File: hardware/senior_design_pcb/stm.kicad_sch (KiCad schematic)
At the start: 53 parts, among them J1 SBH11-PBPC-D05-ST-BK, J10 1x03 Socket, J2 USB_C_Receptacle_USB2.0_16P, J3 1x03 Socket, J4 Conn_01x03_Socket, J5 1x03 Socket, J6 Screw_Terminal_01x06, J7 Screw_Terminal_01x06, J8 Conn_02x08_Odd_Even, J9 Conn_01x03_Socket, SW1 SW_Push, SW2 SW_Push, U1 FT232RL, U2 STM32F091RCTx, U3 LD1117S33TR_SOT223, X1 32.768kHz(12.5pF), X2 8MHz(20pF)

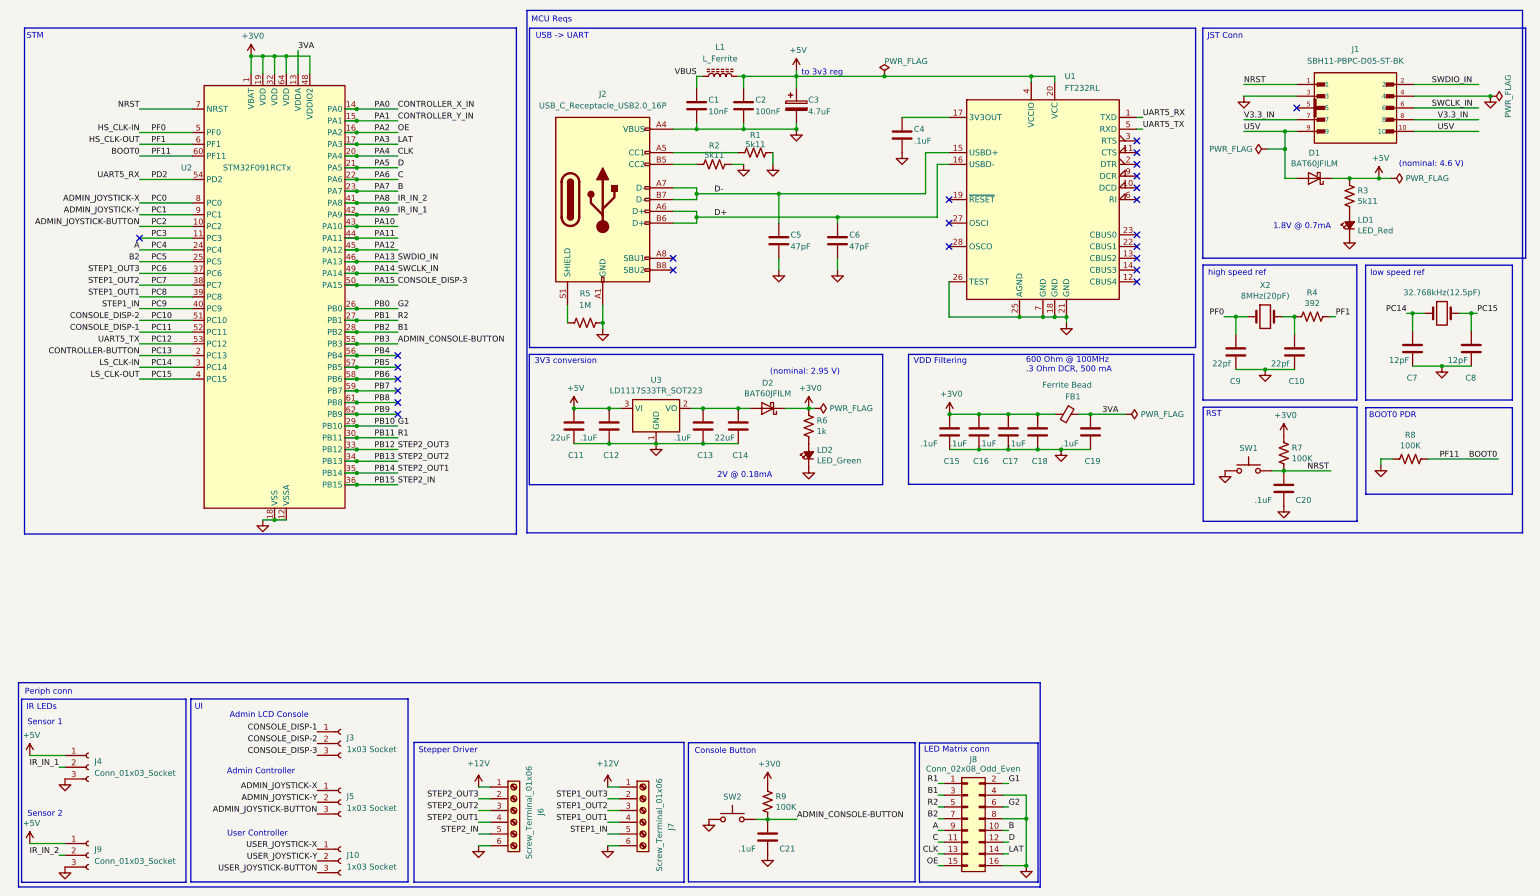
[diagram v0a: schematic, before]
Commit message: vdd caps edited
apparently 362 gaslight us and they dont have the ones we need so i added more :(
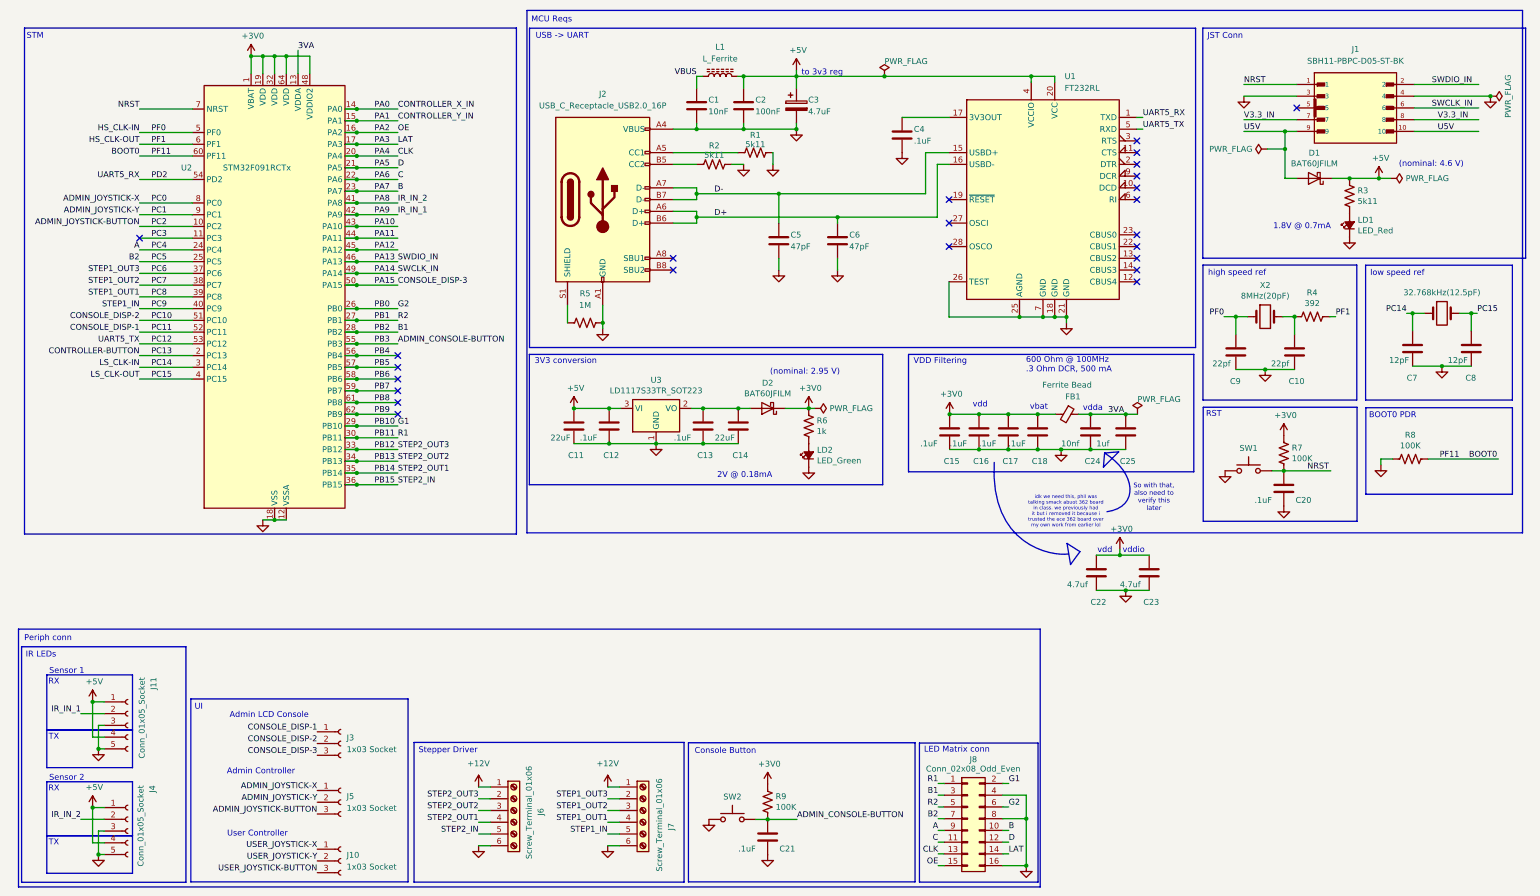
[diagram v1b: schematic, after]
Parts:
- removed C19: .1uF, Capacitor_SMD:C_0805_2012Metric_Pad1.15x1.40mm_HandSolder, symbol Device:C
- removed J4, J9: Conn_01x03_Socket, symbol Connector:Conn_01x03_Socket
- added C22, C23: 4.7uf, Capacitor_SMD:C_0805_2012Metric_Pad1.15x1.40mm_HandSolder, symbol Device:C
- added C24: 10nf, Capacitor_SMD:C_0805_2012Metric_Pad1.15x1.40mm_HandSolder, symbol Device:C
- added C25: 1uf, Capacitor_SMD:C_0805_2012Metric_Pad1.15x1.40mm_HandSolder, symbol Device:C
- added J11, J4: Conn_01x05_Socket, symbol Connector:Conn_01x05_Socket
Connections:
- net +3V0: now also C22.1, C23.1
- net +5V: now also J11.1 (Pin_1), J11.4 (Pin_4), J4.1 (Pin_1), J4.4 (Pin_4)
- net 3VA: now also C24.1, C25.1
- net GND: now also C22.2, C23.2, C24.2, C25.2, J11.3 (Pin_3), J11.5 (Pin_5), J4.3 (Pin_3), J4.5 (Pin_5)
- net IR_IN_1: now also J11.2 (Pin_2)
- net IR_IN_2: now also J4.2 (Pin_2)
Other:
- note added: "RX"
- note added: "So with that, also need to verify this later"
- note added: "TX"
- note added: "idk we need this, phil was talking smack abuot 362 board in class. we previously had it but i removed it because i trusted the ece 362 board over my own work from earlier lol"
- note added: "vbat"
- note added: "vdd"
- note added: "vdd vddio"
- note added: "vdda"

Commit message: fixed connectors
apparently things need power so I added pins for that
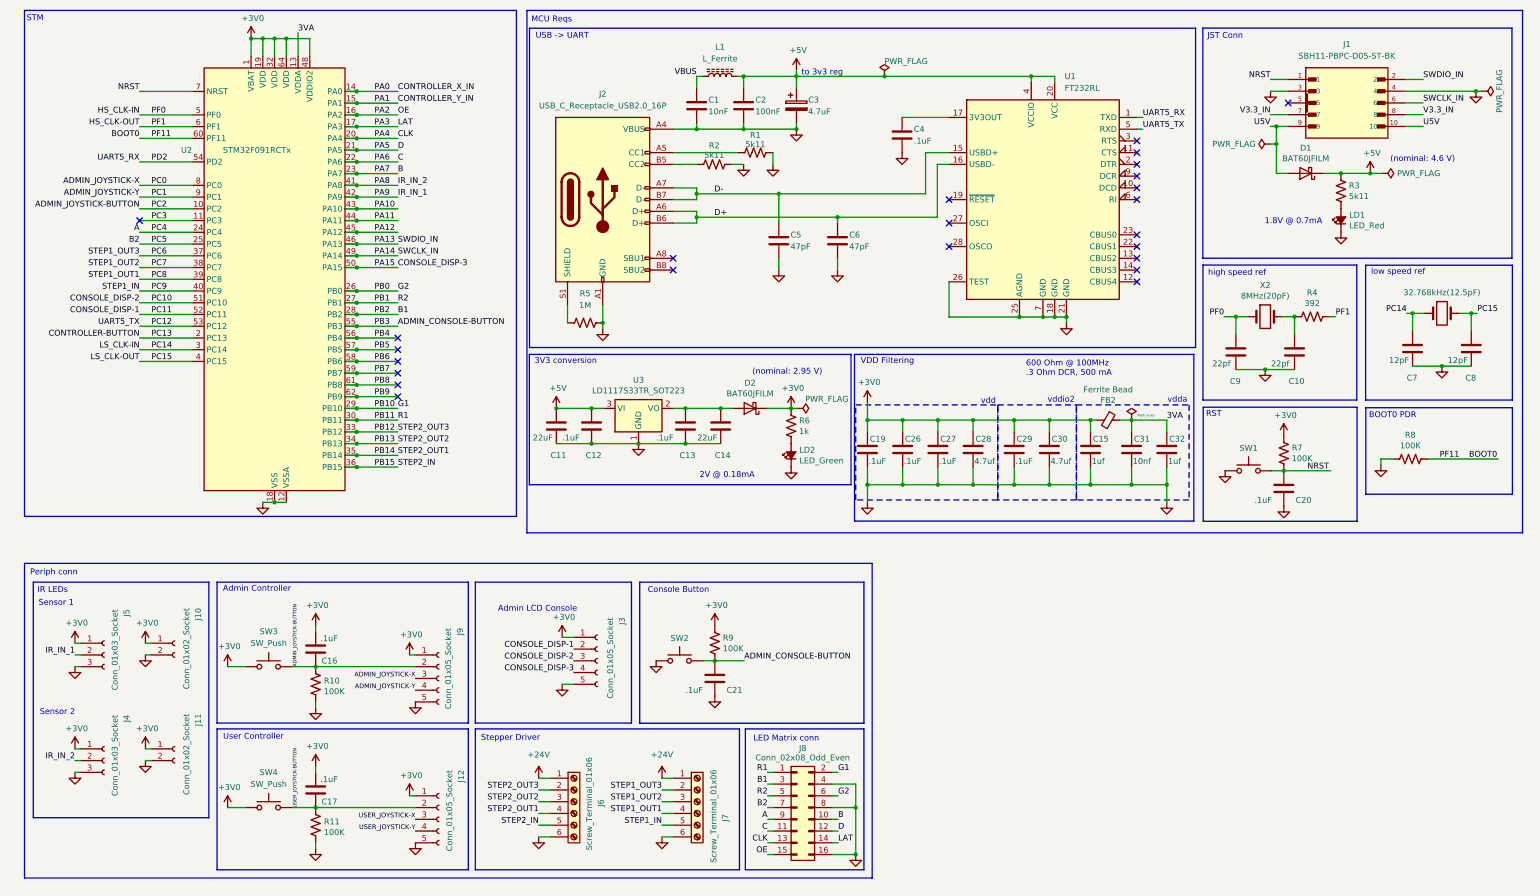
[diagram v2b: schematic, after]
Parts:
- removed C18: .1uF, Capacitor_SMD:C_0805_2012Metric_Pad1.15x1.40mm_HandSolder, symbol Device:C
- removed C22, C23: 4.7uf, Capacitor_SMD:C_0805_2012Metric_Pad1.15x1.40mm_HandSolder, symbol Device:C
- removed C24: 10nf, Capacitor_SMD:C_0805_2012Metric_Pad1.15x1.40mm_HandSolder, symbol Device:C
- removed C25: 1uf, Capacitor_SMD:C_0805_2012Metric_Pad1.15x1.40mm_HandSolder, symbol Device:C
- removed FB1: Ferrite Bead, Inductor_SMD:L_0805_2012Metric_Pad1.15x1.40mm_HandSolder, symbol Device:Ferrite_Bead_Small
- removed J10, J3: 1x03 Socket, symbol Connector:Conn_01x03_Socket
- removed J11, J4: Conn_01x05_Socket, symbol Connector:Conn_01x05_Socket
- added C19, C26, C27, C29: .1uF, Capacitor_SMD:C_0805_2012Metric_Pad1.15x1.40mm_HandSolder, symbol Device:C
- added C28, C30: 4.7uf, Capacitor_SMD:C_0805_2012Metric_Pad1.15x1.40mm_HandSolder, symbol Device:C
- added C31: 10nf, Capacitor_SMD:C_0805_2012Metric_Pad1.15x1.40mm_HandSolder, symbol Device:C
- added C32: 1uf, Capacitor_SMD:C_0805_2012Metric_Pad1.15x1.40mm_HandSolder, symbol Device:C
- added FB2: Ferrite Bead, Inductor_SMD:L_0805_2012Metric_Pad1.15x1.40mm_HandSolder, symbol Device:Ferrite_Bead_Small
- added J10, J11: Conn_01x02_Socket, symbol Connector:Conn_01x02_Socket
- added J12, J3, J9: Conn_01x05_Socket, symbol Connector:Conn_01x05_Socket
- added J4: Conn_01x03_Socket, symbol Connector:Conn_01x03_Socket
- added R10, R11: 100K, Resistor_SMD:R_0805_2012Metric_Pad1.15x1.40mm_HandSolder, symbol Device:R_US
- added SW3, SW4: SW_Push, symbol Switch:SW_Push
- C15: value .1uF -> 1uf
- J5: value 1x03 Socket -> Conn_01x03_Socket
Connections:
- net +3V0: now also J5.1 (Pin_1), C19.1, C26.1, C27.1, C28.1, C29.1, C30.1, FB2.2, J10.1 (Pin_1), J11.1 (Pin_1), J12.1 (Pin_1), J3.1 (Pin_1), J4.1 (Pin_1), J9.1 (Pin_1), SW3.1, SW4.1
- net 3VA: now also C31.1, C32.1, FB2.1
- net ADMIN_JOYSTICK-BUTTON: now also C16.2, J9.2 (Pin_2), R10.1, SW3.2; no longer J5.3 (Pin_3)
- net ADMIN_JOYSTICK-X: now also J9.3 (Pin_3); no longer J5.1 (Pin_1)
- net ADMIN_JOYSTICK-Y: now also J9.4 (Pin_4); no longer J5.2 (Pin_2)
- net CONSOLE_DISP-1: now also J3.2 (Pin_2)
- net CONSOLE_DISP-2: now also J3.3 (Pin_3)
- net CONSOLE_DISP-3: now also J3.4 (Pin_4)
- net GND: now also J5.3 (Pin_3), C19.2, C26.2, C27.2, C28.2, C29.2, C30.2, C31.2, C32.2, J10.2 (Pin_2), J11.2 (Pin_2), J12.5 (Pin_5), J3.5 (Pin_5), J4.3 (Pin_3), J9.5 (Pin_5), R10.2, R11.2; no longer C16.2, C17.2
- net IR_IN_1: now also J5.2 (Pin_2)
- net IR_IN_2: now also J4.2 (Pin_2)
- net USER_JOYSTICK-BUTTON: now also C17.2, J12.2 (Pin_2), R11.1, SW4.2
- net USER_JOYSTICK-X: now also J12.3 (Pin_3)
- net USER_JOYSTICK-Y: now also J12.4 (Pin_4)
- net +12V renamed +24V
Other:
- note added: "vddio2"
- note removed: "RX"
- note removed: "So with that, also need to verify this later"
- note removed: "TX"
- note removed: "UI"
- note removed: "idk we need this, phil was talking smack abuot 362 board in class. we previously had it but i removed it because i trusted the ece 362 board over my own work from earlier lol"
- note removed: "vbat"
- note removed: "vdd vddio"
- moved on the sheet: C11, C12, C13, C14, C21, D1, D2, J1, J6, J7, J8, LD1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

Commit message: Update stm.kicad_sch
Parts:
- removed L1: L_Ferrite, Resistor_SMD:R_0805_2012Metric_Pad1.15x1.40mm_HandSolder, symbol Device:L_Ferrite
- added FB2: Ferrite Bead, Inductor_SMD:L_0805_2012Metric_Pad1.15x1.40mm_HandSolder, symbol Device:Ferrite_Bead_Small
- renumbered C19 to C15, C26 to C16, C27 to C17, C28 to C18, C29 to C19, C30 to C20, C15 to C21, C31 to C22, C32 to C23, C20 to C24, C16 to C25, C21 to C26, C17 to C27, FB2 to FB1, J7 to J10, J8 to J11, J10 to J3, J5 to J4, J3 to J5, J9 to J6, J11 to J7, J4 to J8, J6 to J9
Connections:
- net +5V: now also FB2.1
- net VBUS: now also FB2.2
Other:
- moved on the sheet: C1, C10, C11, C12, C13, C14, C15, C16, C17, C18, C19, C2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

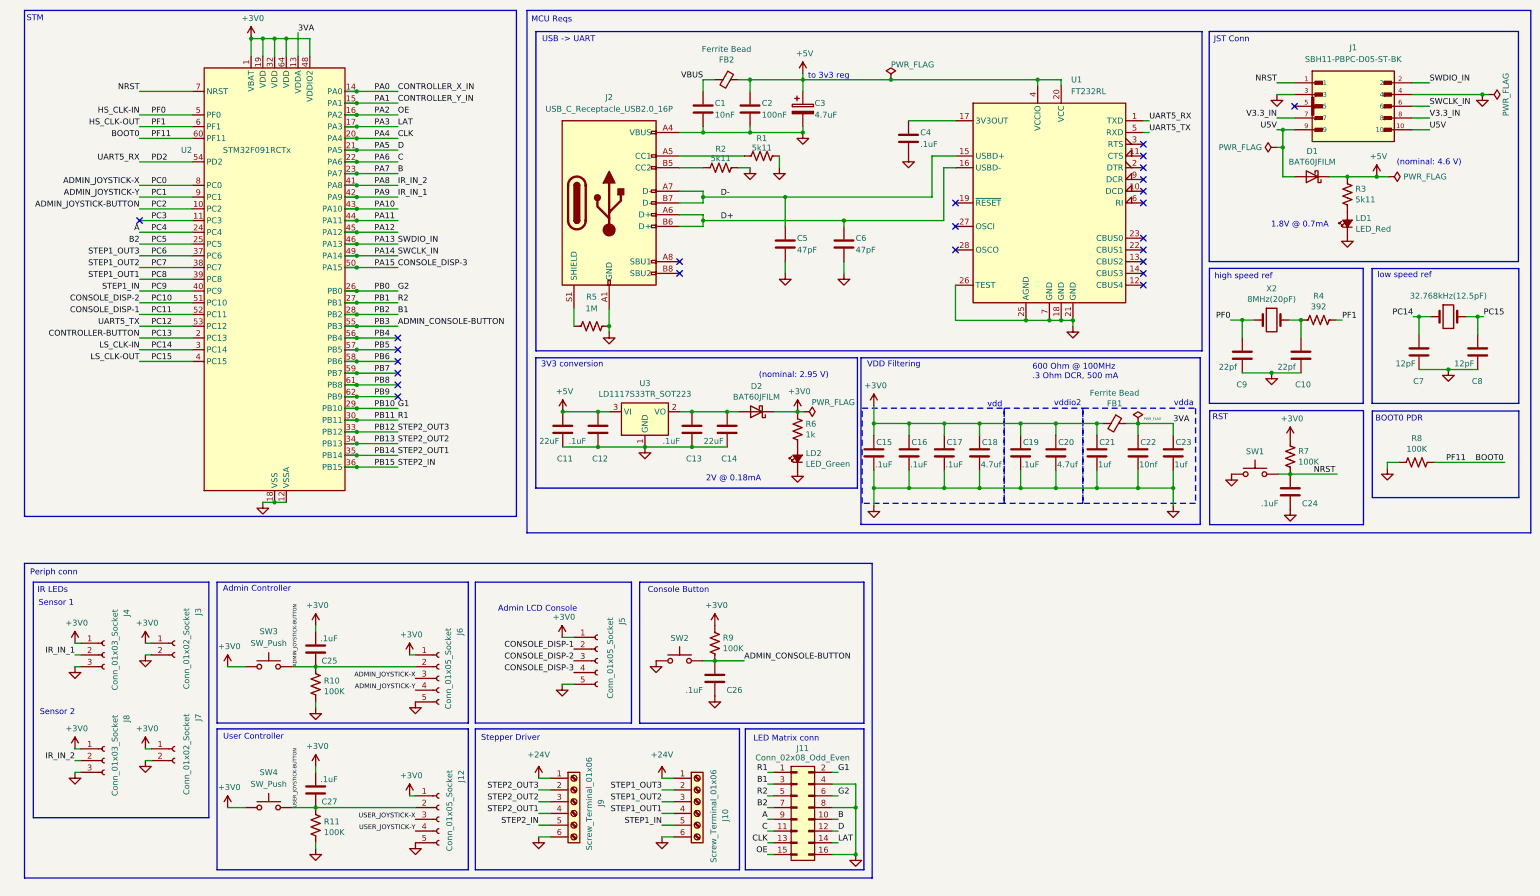
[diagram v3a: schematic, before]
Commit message: annotated. fixed 3v->5v for IR sensors
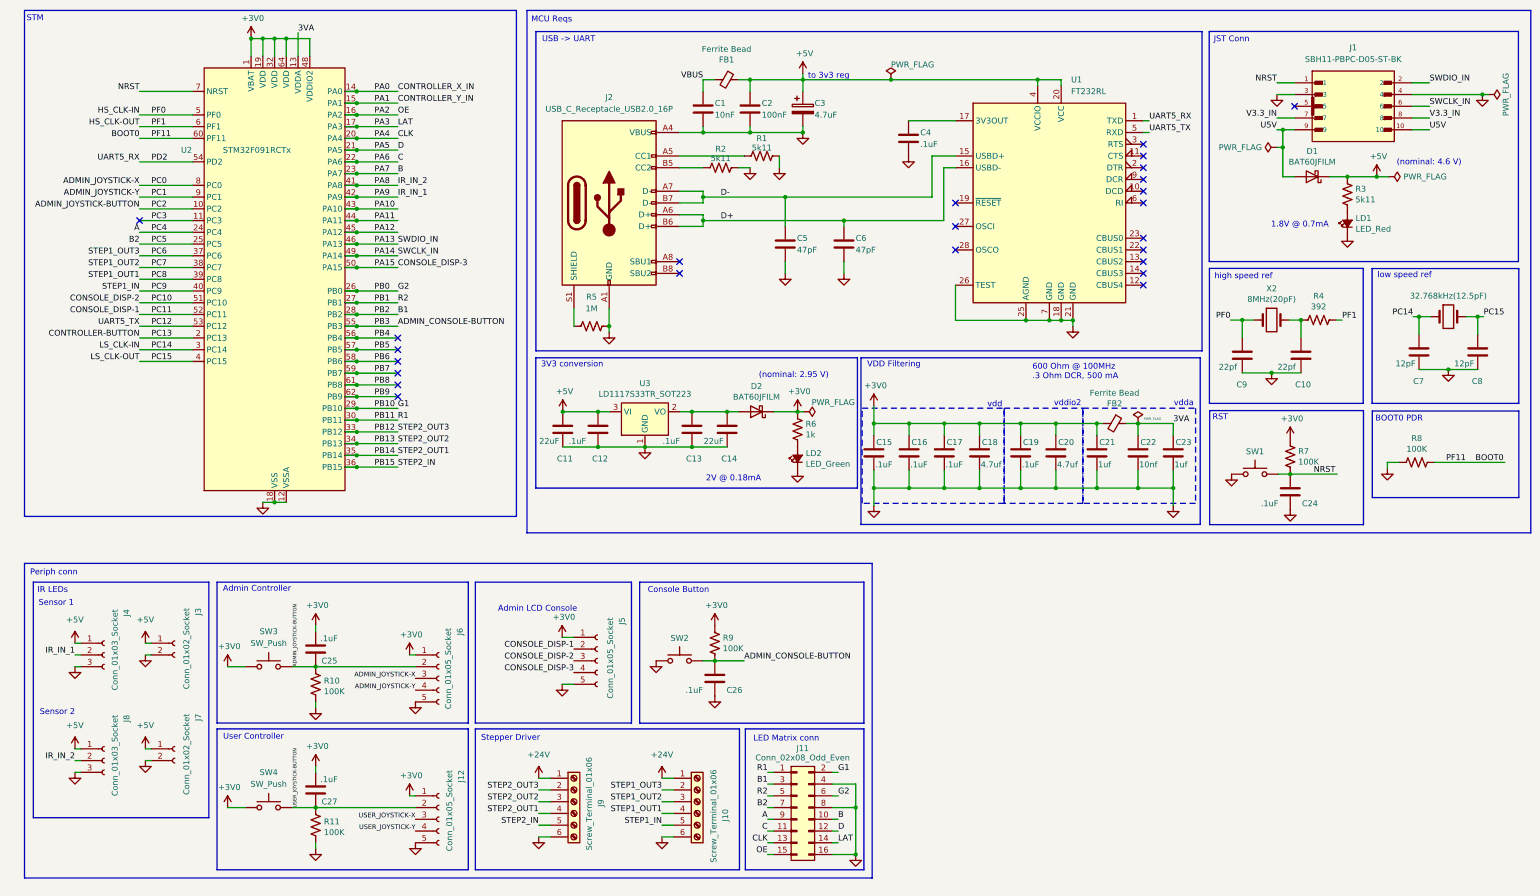
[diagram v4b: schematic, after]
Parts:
- renumbered FB2 to FB1, FB1 to FB2
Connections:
- net +3V0: no longer J3.1 (Pin_1), J4.1 (Pin_1), J7.1 (Pin_1), J8.1 (Pin_1)
- net +5V: now also J3.1 (Pin_1), J4.1 (Pin_1), J7.1 (Pin_1), J8.1 (Pin_1)

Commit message: added comments
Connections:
- net D+: no longer C6.1
- net D-: no longer C5.1
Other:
- moved on the sheet: C5, C6
